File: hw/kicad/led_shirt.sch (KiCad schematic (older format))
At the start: 20 parts, among them J1 10103593-0001LF, P1 b+, P2 b-, Q1 PN_MOSFET_DUAL, SW1 SW_PUSH, U1 PIC12F1822, U2 MCP73831

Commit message: fix labels
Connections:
- net icspclk: no longer J1.4 (ID)
- net icspdat: no longer J1.2 (D-)
- net mclr: no longer J1.3 (D+)
- no-connect marks 1 -> 4
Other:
- moved on the sheet: R1, SW1
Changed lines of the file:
@@
 EESchema Schematic File Version 2
-LIBS:led_shirt-rescue
 LIBS:power
 LIBS:device
@@
 Comment4 ""
 $EndDescr
-Text GLabel 8300 3100 0    60   Input ~ 0
+Text Label 8300 3100 2    60   ~ 0
 vbat
-Text GLabel 4750 2100 0    60   Input ~ 0
+Text Label 5300 3000 0    60   ~ 0
 vbat
 $Comp
 L R-RESCUE-led_shirt R1
 U 1 1 509FF0CA
-P 4850 2450
-F 0 "R1" V 4930 2450 50  0000 C CNN
-F 1 "10kΩ" V 4850 2450 50  0000 C CNN
-F 2 "kicadlib:SMD_0603_R" H 4850 2450 60  0001 C CNN
-F 3 "" H 4850 2450 60  0001 C CNN
-	1    4850 2450
+P 5200 3350
+F 0 "R1" V 5280 3350 50  0000 C CNN
+F 1 "10kΩ" V 5200 3350 50  0000 C CNN
+F 2 "kicadlib:SMD_0603_R" H 5200 3350 60  0001 C CNN
+F 3 "" H 5200 3350 60  0001 C CNN
+	1    5200 3350
 	1    0    0    -1
 $EndComp
@@
 	1    0    0    -1
 $EndComp
-Text GLabel 5700 4000 0    60   Input ~ 0
+Text Label 5700 4000 2    60   ~ 0
 mclr
 $Comp
@@
 	1    0    0    -1
 $EndComp
-Text GLabel 3100 1600 0    60   Input ~ 0
+Text Label 3100 1600 2    60   ~ 0
 vbat
 $Comp
@@
 	1    0    0    -1
 $EndComp
-Text GLabel 8600 1950 2    60   Input ~ 0
+Text Label 8600 1950 0    60   ~ 0
 vbat
-Text GLabel 4150 6150 2    60   Input ~ 0
+Text Label 4150 6150 0    60   ~ 0
 vbat
 $Comp
@@
 	1    0    0    -1
 $EndComp
-Text GLabel 1150 6150 0    60   Input ~ 0
+Text Label 1150 6150 2    60   ~ 0
 vbus
 $Comp
@@
 	1    0    0    -1
 $EndComp
-Text GLabel 1800 1250 2    60   Input ~ 0
+Text Label 1800 1250 0    60   ~ 0
 vbus
 $Comp
@@
 	1    0    0    -1
 $EndComp
-Text GLabel 5750 4750 0    60   Input ~ 0
+Text Label 5750 4750 0    60   ~ 0
 vbat
 $Comp
@@
 Connection ~ 3700 6900
 Wire Wire Line
-	5250 3550 5800 3550
-Wire Wire Line
 	3100 1450 3100 1600
 Wire Wire Line
@@
 L SW_PUSH SW1
 U 1 1 509ED3DD
-P 4450 2850
-F 0 "SW1" H 4600 2960 50  0000 C CNN
-F 1 "SW_PUSH" H 4450 2770 50  0000 C CNN
-F 2 "noah:SW_PB_4PIN_SMT_real" H 4450 2850 60  0001 C CNN
-F 3 "" H 4450 2850 60  0001 C CNN
-	1    4450 2850
-	1    0    0    -1
-$EndComp
-Wire Wire Line
-	4750 2850 4950 2850
+P 5200 4100
+F 0 "SW1" H 5350 4210 50  0000 C CNN
+F 1 "SW_PUSH" H 5200 4020 50  0000 C CNN
+F 2 "noah:SW_PB_4PIN_SMT_real" H 5200 4100 60  0001 C CNN
+F 3 "" H 5200 4100 60  0001 C CNN
+	1    5200 4100
+	0    -1   -1   0
+$EndComp
 $Comp
 L GND-RESCUE-led_shirt #PWR06
 U 1 1 56338053
-P 4000 2950
-F 0 "#PWR06" H 4000 2950 30  0001 C CNN
-F 1 "GND" H 4000 2880 30  0001 C CNN
-F 2 "" H 4000 2950 60  0001 C CNN
-F 3 "" H 4000 2950 60  0001 C CNN
-	1    4000 2950
-	1    0    0    -1
-$EndComp
-Connection ~ 4850 2850
-Wire Wire Line
-	4000 2850 4150 2850
-Wire Wire Line
-	5250 3050 5250 3550
-Wire Wire Line
-	4850 3700 5800 3700
-Text GLabel 1800 1450 2    60   Input ~ 0
-mclr
-Text GLabel 7100 3700 2    60   Input ~ 0
+P 5200 4500
+F 0 "#PWR06" H 5200 4500 30  0001 C CNN
+F 1 "GND" H 5200 4430 30  0001 C CNN
+F 2 "" H 5200 4500 60  0001 C CNN
+F 3 "" H 5200 4500 60  0001 C CNN
+	1    5200 4500
+	1    0    0    -1
+$EndComp
+Text Label 7100 3700 0    60   ~ 0
 icspdat
-Text GLabel 7100 3850 2    60   Input ~ 0
+Text Label 7100 3850 0    60   ~ 0
 icspclk
 Wire Wire Line
@@
 Wire Wire Line
 	7100 3850 7000 3850
-Text GLabel 2050 1350 2    60   Input ~ 0
-icspdat
-Text GLabel 2050 1550 2    60   Input ~ 0
-icspclk
-Wire Wire Line
-	2050 1350 1650 1350
-Wire Wire Line
-	1800 1450 1650 1450
-Wire Wire Line
-	1650 1550 2050 1550
 $Comp
 L PN_MOSFET_DUAL Q1
@@
 	1    0    0    -1
 $EndComp
-Text GLabel 7200 4000 2    60   Input ~ 0
+Text Label 7200 4000 0    60   ~ 0
 Q1_G
-Text GLabel 8400 4500 0    60   Input ~ 0
+Text Label 8400 4500 0    60   ~ 0
 Q1_D
-Text GLabel 4950 2850 2    60   Input ~ 0
+Text Label 5100 3700 2    60   ~ 0
 Q2_G
-Text GLabel 5250 3050 2    60   Input ~ 0
+Text Label 5700 3550 2    60   ~ 0
 Q2_S
-Text GLabel 8600 1050 2    60   Input ~ 0
+Text Label 8600 1050 0    60   ~ 0
 Q1_D
-Text GLabel 7100 1050 0    60   Input ~ 0
+Text Label 7100 1050 2    60   ~ 0
 Q1_G
-Text GLabel 7100 1950 0    60   Input ~ 0
+Text Label 7100 1950 2    60   ~ 0
 Q2_G
-Text GLabel 7100 1500 0    60   Input ~ 0
+Text Label 7100 1500 2    60   ~ 0
 Q2_S
 Wire Wire Line
@@
 	8500 1950 8600 1950
 Wire Wire Line
-	4000 2950 4000 2850
-Wire Wire Line
-	4750 2100 4850 2100
-Wire Wire Line
-	4850 2100 4850 2200
-Wire Wire Line
-	4850 2700 4850 3700
+	5200 3000 5200 3100
 $Comp
 L GND-RESCUE-led_shirt #PWR07
@@
 	7000 4000 7200 4000
 Connection ~ 7100 4000
+NoConn ~ 1650 1350
+NoConn ~ 1650 1450
+NoConn ~ 1650 1550
+Wire Wire Line
+	5300 3000 5200 3000
+Wire Wire Line
+	5700 3550 5800 3550
+Wire Wire Line
+	5100 3700 5800 3700
+Wire Wire Line
+	5200 4500 5200 4400
+Wire Wire Line
+	5200 3600 5200 3800
+Connection ~ 5200 3700
 $EndSCHEMATC

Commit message: finish sch, add bom
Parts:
- removed D1, D2, D3, D4: LED, kicadlib:plcc2, symbol LED-RESCUE-led_shirt
- removed P1: b+, noah:noah_hole_1, symbol TST
- removed P2: b-, noah:noah_hole_1, symbol TST
- added C1: 1.0µF, kicadlib:SMD_0603_R, symbol C-RESCUE-led_shirt
- added D1: D_Schottky, symbol D_Schottky
- added J2, J3: 2_PIN_HDR, symbol 2_PIN_HDR
- added J4: 5_PIN_HDR, symbol 5_PIN_HDR
- added L1: INDUCTOR, symbol INDUCTOR
- added R1, R2, R4, R6: 10kΩ, kicadlib:SMD_0603_R, symbol R-RESCUE-led_shirt
- added U1: AP3012, symbol AP3012
- renumbered C1 to C2, C2 to C3, D5 to D2, R6 to R10, R1 to R3, R2 to R5, R3 to R7, R4 to R8, R5 to R9, U1 to U2, U2 to U3
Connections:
- net GND: now also C1.2, J2.2, J4.5, R2.2, R6.2, U1.2 (GND)
- net icspclk: now also J4.3
- net icspdat: now also J4.2
- net mclr: now also J4.4
- net vbat: now also J2.1, L1.2, U1.5 (VIN)
- net led-: now reaches R5.1
- net led-: now also J3.2
- net batt_sns: now reaches U2.3 (RA4)
- net batt_sns: now also R4.2, R6.1
- net Q1_D: no longer names the net of Q1.6 (D1), R5.2
- net Q1_G renamed led_cntrl
- net Q2_G renamed ~lps_enable
- net Q2_S renamed lps
- net lps: now also J4.1, R4.1, U1.4 (~SHDN)
- new net: D1.2 (A), L1.1, U1.1 (SW)
- new net: R1.2, R2.1, U1.3 (FB)
- new net +12v: C1.1, D1.1 (K), J3.1, R1.1
- no-connect marks 4 -> 3
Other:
- note added: "*LPS output also\nused for 12v enable"
- note added: "+12v Supply"
- note added: "Battery Connector"
- note added: "Control"
- note added: "LED Output"
- note added: "Lipo Charger"
- note added: "Micro USB B Connector"
- note added: "Programming Connector"
- note added: "nopop"
- moved on the sheet: J1, Q1, R3, R5, R7, R8, SW1, U2

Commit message: more components
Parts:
- J4: footprint (none) -> kicadlib:SMD_JST_5_PIN_VERT
- SW1: footprint noah:SW_PB_4PIN_SMT_real -> kicadlib:spst_pushbutton_smd
- U1: footprint (none) -> kicadlib:SMD_SOT23-5
- U2: footprint noah:PIC12F1822-SOIC-8 -> kicadlib:SMD_SOIC-8
- U3: footprint kicadlib:MCP73831 -> kicadlib:SMD_SOT23-5
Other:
- note added: "LPS/Load Switches"
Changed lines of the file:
@@
 LIBS:contrib
 LIBS:valves
-LIBS:noah
 LIBS:extra
 LIBS:kicadlib
@@
 F 0 "U3" H 2650 6000 60  0000 C CNN
 F 1 "MCP73831" H 2650 6600 60  0000 C CNN
-F 2 "kicadlib:MCP73831" H 2650 6300 60  0001 C CNN
+F 2 "kicadlib:SMD_SOT23-5" H 2650 6300 60  0001 C CNN
 F 3 "" H 2650 6300 60  0001 C CNN
 	1    2650 6300
@@
 F 0 "U2" H 3250 3450 60  0000 C CNN
 F 1 "PIC12F1822" H 3250 4300 60  0000 C CNN
-F 2 "noah:PIC12F1822-SOIC-8" H 3300 3850 60  0001 C CNN
+F 2 "kicadlib:SMD_SOIC-8" H 3300 3850 60  0001 C CNN
 F 3 "" H 3300 3850 60  0000 C CNN
 	1    3250 3900
@@
 F 0 "SW1" H 2200 4360 50  0000 C CNN
 F 1 "SW_PUSH" H 2050 4170 50  0000 C CNN
-F 2 "noah:SW_PB_4PIN_SMT_real" H 2050 4250 60  0001 C CNN
+F 2 "kicadlib:spst_pushbutton_smd" H 2050 4250 60  0001 C CNN
 F 3 "" H 2050 4250 60  0001 C CNN
 	1    2050 4250
@@
 F 0 "U1" H 6800 1500 60  0000 C CNN
 F 1 "AP3012" H 6800 2100 60  0000 C CNN
-F 2 "" H 6750 1800 60  0000 C CNN
+F 2 "kicadlib:SMD_SOT23-5" H 6750 1800 60  0001 C CNN
 F 3 "" H 6750 1800 60  0000 C CNN
 	1    6800 1800
@@
 F 0 "J4" H 5300 4350 60  0000 C CNN
 F 1 "5_PIN_HDR" H 5300 5250 60  0000 C CNN
-F 2 "" H 5300 4800 60  0000 C CNN
+F 2 "kicadlib:SMD_JST_5_PIN_VERT" H 5300 4800 60  0001 C CNN
 F 3 "" H 5300 4800 60  0000 C CNN
 	1    5300 4800
@@
 F 0 "D1" H 6050 1300 50  0000 C CNN
 F 1 "D_Schottky" H 6050 1100 50  0000 C CNN
-F 2 "" H 6050 1200 60  0000 C CNN
+F 2 "" H 6050 1200 60  0001 C CNN
 F 3 "" H 6050 1200 60  0000 C CNN
 	1    6050 1200
@@
 F 0 "L1" V 6750 1200 50  0000 C CNN
 F 1 "INDUCTOR" V 6900 1200 50  0000 C CNN
-F 2 "" H 6800 1200 60  0000 C CNN
+F 2 "" H 6800 1200 60  0001 C CNN
 F 3 "" H 6800 1200 60  0000 C CNN
 	1    6800 1200
@@
 F 0 "J2" H 2400 1350 60  0000 C CNN
 F 1 "2_PIN_HDR" H 2400 1800 60  0000 C CNN
-F 2 "" H 2400 1500 60  0000 C CNN
+F 2 "" H 2400 1500 60  0001 C CNN
 F 3 "" H 2400 1500 60  0000 C CNN
 	1    2400 1500
@@
 F 0 "J3" H 9600 3550 60  0000 C CNN
 F 1 "2_PIN_HDR" H 9600 4000 60  0000 C CNN
-F 2 "" H 9600 3700 60  0000 C CNN
+F 2 "" H 9600 3700 60  0001 C CNN
 F 3 "" H 9600 3700 60  0000 C CNN
 	1    9600 3700
@@
 Text Notes 9450 3250 0    60   ~ 0
 LED Output
+Text Notes 6900 3700 0    60   ~ 0
+LPS/Load Switches
 $EndSCHEMATC

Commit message: footprints mostly done, some missing modules
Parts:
- added C4: CP1, kicadlib:SMD_5X5.2_CAP, symbol CP1
- D1: footprint (none) -> kicadlib:SMD_SOD-123_DIODE
- J2, J3: footprint (none) -> kicadlib:SMD_JST_2_PIN_VERT
- L1: footprint (none) -> kicadlib:SMD_IND_6.8x6.8_SRR6038-100Y
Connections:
- net +12v: now also C4.1
- net GND: now also C4.2
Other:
- note added: "*nopop-\nextra holdup\non +12V"
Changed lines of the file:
@@
 F 0 "D1" H 6050 1300 50  0000 C CNN
 F 1 "D_Schottky" H 6050 1100 50  0000 C CNN
-F 2 "" H 6050 1200 60  0001 C CNN
+F 2 "kicadlib:SMD_SOD-123_DIODE" H 6050 1200 60  0001 C CNN
 F 3 "" H 6050 1200 60  0000 C CNN
 	1    6050 1200
@@
 F 0 "L1" V 6750 1200 50  0000 C CNN
 F 1 "INDUCTOR" V 6900 1200 50  0000 C CNN
-F 2 "" H 6800 1200 60  0001 C CNN
+F 2 "kicadlib:SMD_IND_6.8x6.8_SRR6038-100Y" H 6800 1200 60  0001 C CNN
 F 3 "" H 6800 1200 60  0000 C CNN
 	1    6800 1200
@@
 F 0 "J2" H 2400 1350 60  0000 C CNN
 F 1 "2_PIN_HDR" H 2400 1800 60  0000 C CNN
-F 2 "" H 2400 1500 60  0001 C CNN
+F 2 "kicadlib:SMD_JST_2_PIN_VERT" H 2400 1500 60  0001 C CNN
 F 3 "" H 2400 1500 60  0000 C CNN
 	1    2400 1500
@@
 Connection ~ 6300 1200
 Wire Wire Line
-	5750 1400 5750 1200
-Wire Wire Line
-	5250 1200 5900 1200
+	5750 1200 5750 1400
+Wire Wire Line
+	4650 1200 5900 1200
 Wire Wire Line
 	5750 1950 6350 1950
@@
 	5750 2600 5750 2500
 Wire Wire Line
-	5350 2600 5750 2600
+	5000 2600 5750 2600
 Connection ~ 5550 2600
 Wire Wire Line
@@
 Text Label 7400 1650 0    60   ~ 0
 vbat
-Text Label 5250 1200 2    60   ~ 0
+Text Label 4650 1200 2    60   ~ 0
 +12v
 Wire Wire Line
@@
 F 0 "J3" H 9600 3550 60  0000 C CNN
 F 1 "2_PIN_HDR" H 9600 4000 60  0000 C CNN
-F 2 "" H 9600 3700 60  0001 C CNN
+F 2 "kicadlib:SMD_JST_2_PIN_VERT" H 9600 3700 60  0001 C CNN
 F 3 "" H 9600 3700 60  0000 C CNN
 	1    9600 3700
@@
 Text Notes 6900 3700 0    60   ~ 0
 LPS/Load Switches
+$Comp
+L CP1 C4
+U 1 1 564507C5
+P 5000 1850
+F 0 "C4" H 5025 1950 50  0000 L CNN
+F 1 "CP1" H 5025 1750 50  0000 L CNN
+F 2 "kicadlib:SMD_5X5.2_CAP" H 5000 1850 60  0001 C CNN
+F 3 "" H 5000 1850 60  0000 C CNN
+	1    5000 1850
+	1    0    0    -1
+$EndComp
+Wire Wire Line
+	5000 1700 5000 1200
+Connection ~ 5000 1200
+Wire Wire Line
+	5000 2000 5000 2600
+Connection ~ 5350 2600
+Wire Notes Line
+	4750 1450 4750 2250
+Wire Notes Line
+	4750 2250 5200 2250
+Wire Notes Line
+	5200 2250 5200 1450
+Wire Notes Line
+	5200 1450 4750 1450
+Text Notes 4100 1950 0    60   ~ 0
+*nopop-\nextra holdup\non +12V
 $EndSCHEMATC

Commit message: parts positioned, silks. next is traces.
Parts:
- J2, J3: footprint kicadlib:SMD_JST_2_PIN_VERT -> kicadlib:TH_JST_2PIN_RIGHTANGLE
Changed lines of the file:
@@
 F 0 "J2" H 2400 1350 60  0000 C CNN
 F 1 "2_PIN_HDR" H 2400 1800 60  0000 C CNN
-F 2 "kicadlib:SMD_JST_2_PIN_VERT" H 2400 1500 60  0001 C CNN
+F 2 "kicadlib:TH_JST_2PIN_RIGHTANGLE" H 2400 1500 60  0001 C CNN
 F 3 "" H 2400 1500 60  0000 C CNN
 	1    2400 1500
@@
 F 0 "J3" H 9600 3550 60  0000 C CNN
 F 1 "2_PIN_HDR" H 9600 4000 60  0000 C CNN
-F 2 "kicadlib:SMD_JST_2_PIN_VERT" H 9600 3700 60  0001 C CNN
+F 2 "kicadlib:TH_JST_2PIN_RIGHTANGLE" H 9600 3700 60  0001 C CNN
 F 3 "" H 9600 3700 60  0000 C CNN
 	1    9600 3700

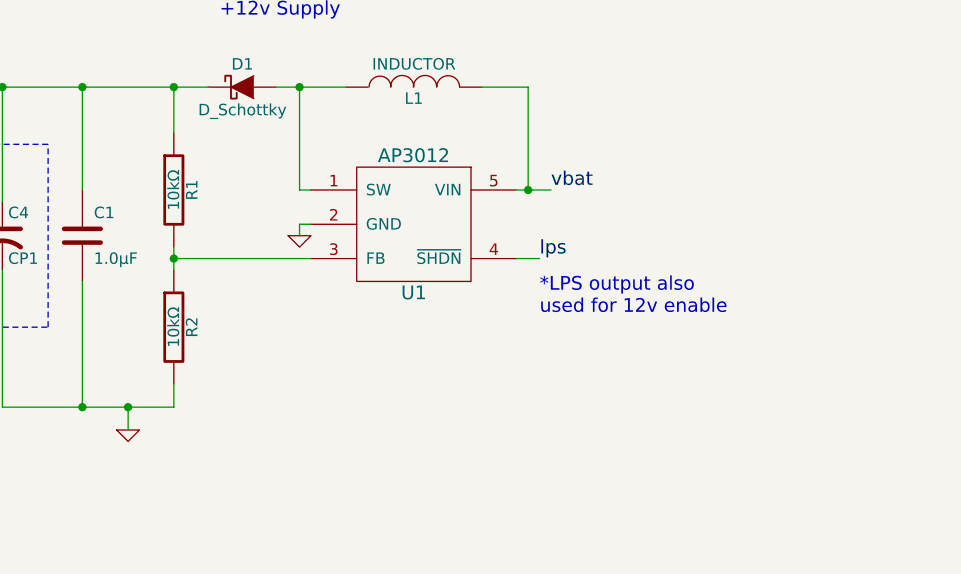
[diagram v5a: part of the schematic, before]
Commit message: update 12v boost feedback resistor divider
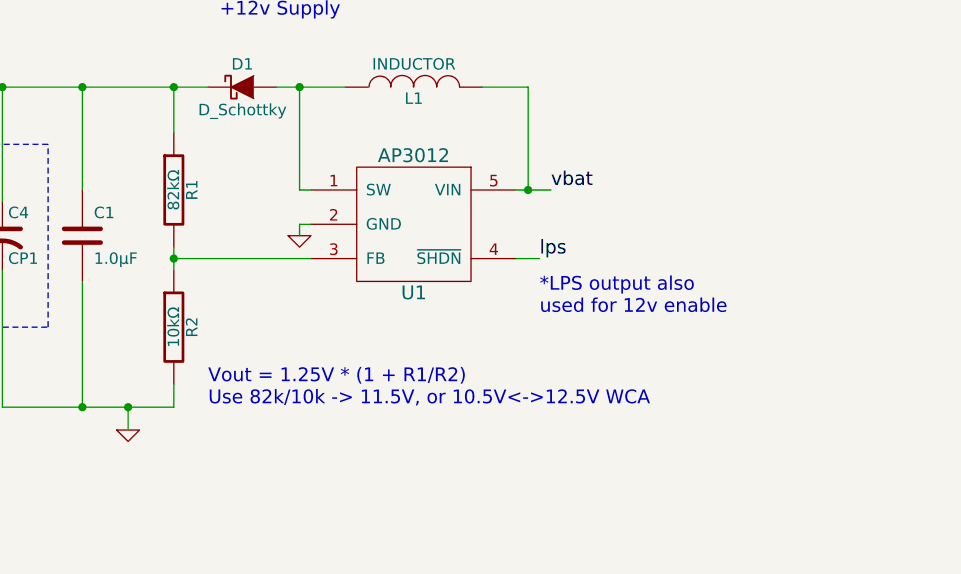
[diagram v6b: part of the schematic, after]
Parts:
- R1: value 10kΩ -> 82kΩ
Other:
- note added: "Vout = 1.25V * (1 + R1/R2)\nUse 82k/10k -> 11.5V, or 10.5V<->12.5V WCA"
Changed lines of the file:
@@
 P 5750 1650
 F 0 "R1" V 5830 1650 50  0000 C CNN
-F 1 "10kΩ" V 5750 1650 50  0000 C CNN
+F 1 "82kΩ" V 5750 1650 50  0000 C CNN
 F 2 "kicadlib:SMD_0603_R" H 5750 1650 60  0001 C CNN
 F 3 "" H 5750 1650 60  0001 C CNN
@@
 Text Notes 4100 1950 0    60   ~ 0
 *nopop-\nextra holdup\non +12V
+Text Notes 5900 2600 0    60   ~ 0
+Vout = 1.25V * (1 + R1/R2)\nUse 82k/10k -> 11.5V, or 10.5V<->12.5V WCA
 $EndSCHEMATC
